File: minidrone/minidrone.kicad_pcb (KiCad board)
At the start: 2 copper layers, 45 x 150 mm, 88 parts, among them J1 GATE, J2 OUT, J3 Conn_01x10, Q1 BC337, Q2 BC337, Q3 BC337, Q4 BC337, Q5 BC337, Q6 BC377, Q7 BC377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

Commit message: Correct pot footprints. continue layout
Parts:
- R10, R2, R4, R6, R8: footprint Resistor_THT:R_Axial_DIN0207_L6.3mm_D2.5mm_P10.16mm_Horizontal -> Resistor_THT:R_Axial_DIN0207_L6.3mm_D2.5mm_P2.54mm_Vertical
- R13: value 10k -> 100k
- R15: value 47k -> 330k
- R16: footprint Resistor_THT:R_Axial_DIN0207_L6.3mm_D2.5mm_P2.54mm_Vertical -> Resistor_THT:R_Axial_DIN0207_L6.3mm_D2.5mm_P10.16mm_Horizontal
- RV1, RV2, RV3, RV4, RV5, RV6: footprint Potentiometer_THT:Potentiometer_Bourns_PTV09A-1_Single_Vertical -> minidrone:Bourns_PVT09A
- RV7, RV8: footprint Potentiometer_THT:Potentiometer_Bourns_PTV09A-1_Single_Vertical -> minidrone:Bourns_PDB12-H
- moved R11 235.9 mm to (-105.0, 147.0)
- moved R14 235.9 mm to (-107.5, 199.1)
- moved C9 225.2 mm to (148.0, 189.8), turned to 0 degrees
- moved C13 197.4 mm to (140.9, 147.2)
- moved C12 194.9 mm to (128.3, 157.4)
- moved C8 189.1 mm to (140.3, 189.8), turned to 0 degrees
- moved Q6 166.3 mm to (126.3, 130.7), turned to 90 degrees
- moved J2 99.0 mm to (153.7, 86.3)
- moved RV6 77.8 mm to (147.9, 104.7), turned to 0 degrees
- moved SW5 69.9 mm to (104.8, 189.1)
- moved SW4 66.1 mm to (104.8, 165.0)
- moved D5 65.2 mm to (116.2, 189.1), turned to 180 degrees
- moved SW3 62.4 mm to (104.8, 140.9)
- moved R10 61.5 mm to (55.0, 188.1)
- moved R4 61.5 mm to (55.0, 128.1)
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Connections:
- net /Oscillator Bank/VIN renamed /VIN
- C10 pad 2: Net-(C10-Pad2) -> GND
- C11 pad 1: Net-(C10-Pad2) -> GND
- C12 pad 2: Net-(C12-Pad2) -> GND
- C13 pad 1: Net-(C12-Pad2) -> GND
- C14 pad 2: Net-(C14-Pad2) -> GND
- C15 pad 1: Net-(C14-Pad2) -> GND
- C7 pad 1: Net-(C7-Pad1) -> /EG_CAP
- D6 pad 1: Net-(D6-Pad1) -> /EG_TRIG
- D7 pad 1: Net-(D6-Pad1) -> /EG_TRIG
- D8 pad 2: Net-(D8-Pad2) -> /EG_COMP_OUT
- D9 pad 1: Net-(D8-Pad2) -> /EG_COMP_OUT
- R13 pad 1: Net-(R13-Pad1) -> /EG_CREF
- R14 pad 1: Net-(D6-Pad1) -> /EG_TRIG
- R15 pad 2: Net-(R13-Pad1) -> /EG_CREF
- RV7 pad 2: Net-(C7-Pad1) -> /EG_CAP
- RV7 pad 3: Net-(C7-Pad1) -> /EG_CAP
- RV8 pad 2: Net-(C7-Pad1) -> /EG_CAP
- RV8 pad 3: Net-(C7-Pad1) -> /EG_CAP
- U2 pad 1: Net-(D8-Pad2) -> /EG_OUT
- U2 pad 2: Net-(R13-Pad1) -> /EG_OUT
- U2 pad 3: Net-(D6-Pad1) -> /EG_CAP
- U2 pad 5: Net-(C7-Pad1) -> /EG_TRIG
- U2 pad 6: /EG_OUT -> /EG_CREF
- U2 pad 7: /EG_OUT -> /EG_COMP_OUT
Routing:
- net /VIN: track 0.00 -> 147.3 mm
- net /EG_CAP: track 0.00 -> 31.6 mm
- net Net-(D8-Pad1): track 0.00 -> 29.4 mm
- net Net-(R1-Pad1): track 0.00 -> 26.8 mm
- net Net-(D7-Pad2): track 0.00 -> 17.4 mm
- net /EG_COMP_OUT: track 0.00 -> 15.0 mm
- net /GATE: track 0.00 -> 13.1 mm
- net Net-(C1-Pad1): track 0.00 -> 12.5 mm
- net Net-(C1-Pad2): track 0.00 -> 9.56 mm
- net Net-(Q6-Pad2): track 0.00 -> 8.46 mm
- net Net-(D9-Pad2): track 0.00 -> 7.06 mm
- net /EG_OUT: track 0.00 -> 6.88 mm
- net +12V: track 0.00 -> 5.61 mm
- net Net-(R1-Pad2): track 0.00 -> 5.22 mm
- net /EG_TRIG: track 0.00 -> 5.08 mm
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- added copper zone on B.Cu, net +12V
- added copper zone on B.Cu, net -12V
- added copper zone on F.Cu, net GND
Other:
- board size 45 x 150 mm -> 61 x 124.5 mm

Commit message: Continue layout
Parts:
- R10, R11, R13, R17, R18, R19, R2, R20, R24, R4, R6, R8: footprint Resistor_THT:R_Axial_DIN0207_L6.3mm_D2.5mm_P2.54mm_Vertical -> Resistor_THT:R_Axial_DIN0207_L6.3mm_D2.5mm_P10.16mm_Horizontal
- R14: value 100k -> 330k; footprint Resistor_THT:R_Axial_DIN0207_L6.3mm_D2.5mm_P2.54mm_Vertical -> Resistor_THT:R_Axial_DIN0207_L6.3mm_D2.5mm_P10.16mm_Horizontal
- R15: value 330k -> 100k
- moved R23 322.4 mm to (209.3, -42.2)
- moved R25 322.4 mm to (211.5, -34.1)
- moved R28 322.4 mm to (224.8, -23.8)
- moved R14 317.5 mm to (196.2, 106.8), turned to 180 degrees
- moved C15 311.8 mm to (212.1, 48.9), turned to 0 degrees
- moved C14 306.2 mm to (207.0, 36.2), turned to 0 degrees
- moved R19 304.8 mm to (224.2, 38.7), turned to -90 degrees
- moved R11 302.4 mm to (190.5, 82.6)
- moved R18 295.8 mm to (217.2, 38.7), turned to -90 degrees
- moved R21 285.6 mm to (201.3, 75.0), turned to 90 degrees
- moved Q9 282.3 mm to (199.8, 54.7), turned to -90 degrees
- moved R24 280.9 mm to (232.4, 52.7), turned to 90 degrees
- moved R30 278.8 mm to (218.7, 66.7), turned to 0 degrees
- moved Q8 273.9 mm to (203.2, 59.8), turned to 90 degrees
- moved JP1 273.9 mm to (195.6, 57.1), turned to 0 degrees
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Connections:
- R14 pad 1: /EG_TRIG -> +12V
- R14 pad 2: GND -> /EG_CREF
- R15 pad 1: +12V -> /EG_TRIG
- R15 pad 2: /EG_CREF -> GND
- U3 pad 1: Net-(R29-Pad2) -> Net-(R20-Pad2)
- U3 pad 2: Net-(R26-Pad2) -> Net-(R17-Pad2)
- U3 pad 3: Net-(R27-Pad2) -> Net-(R18-Pad1)
- U3 pad 5: Net-(R18-Pad1) -> Net-(R27-Pad2)
- U3 pad 6: Net-(R17-Pad2) -> Net-(R26-Pad2)
- U3 pad 7: Net-(R20-Pad2) -> Net-(R29-Pad2)
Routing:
- net -12V: track 0.00 -> 188.9 mm
- net +12V: track 5.61 -> 140.9 mm
- net /Oscillator Bank/OUT: track 0.00 -> 83.3 mm, vias 0 -> 1
- net Net-(R17-Pad2): track 0.00 -> 54.7 mm
- net Net-(C6-Pad1): track 0.00 -> 30.1 mm
- net Net-(C5-Pad1): track 0.00 -> 30.0 mm
- net Net-(RV6-Pad2): track 0.00 -> 29.5 mm
- net Net-(R3-Pad1): track 0.00 -> 25.0 mm
- net /EG_OUT: track 6.88 -> 28.9 mm
- net /EG_CREF: track 0.00 -> 20.9 mm
- net /EG_CAP: track 31.6 -> 52.4 mm
- net Net-(C2-Pad1): track 0.00 -> 20.6 mm
- net Net-(R9-Pad1): track 0.00 -> 20.1 mm
- net Net-(C3-Pad1): track 0.00 -> 19.9 mm
- net Net-(C4-Pad1): track 0.00 -> 19.7 mm
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- removed copper zone on B.Cu, net +12V
- removed copper zone on B.Cu, net -12V
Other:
- board size 61 x 124.5 mm -> 61 x 116.8 mm

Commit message: Complete layout
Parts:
- R12, R15, R21, R22, R25, R26, R27, R28, R29, R30: footprint Resistor_THT:R_Axial_DIN0207_L6.3mm_D2.5mm_P2.54mm_Vertical -> Resistor_THT:R_Axial_DIN0207_L6.3mm_D2.5mm_P10.16mm_Horizontal
- R23: value 20k 0.1% -> 10k; footprint Resistor_THT:R_Axial_DIN0207_L6.3mm_D2.5mm_P2.54mm_Vertical -> Resistor_THT:R_Axial_DIN0207_L6.3mm_D2.5mm_P10.16mm_Horizontal
- R24: value 10k -> 20k 0.1%
- moved R25 105.3 mm to (206.4, 71.1), turned to 90 degrees
- moved R23 90.7 mm to (216.5, 48.3), turned to 90 degrees
- moved R28 73.2 mm to (203.8, 46.4), turned to 90 degrees
- moved J2 49.1 mm to (184.2, 38.1), turned to 180 degrees
- moved R24 43.9 mm to (188.6, 55.9), turned to 0 degrees
- moved R30 36.8 mm to (198.1, 36.2), turned to 180 degrees
- moved R3 19.3 mm to (177.8, 75.6), turned to 90 degrees
- moved R26 18.5 mm to (188.6, 53.3)
- moved JP1 11.0 mm to (184.8, 59.1), turned to 90 degrees
- moved R27 9.44 mm to (206.4, 58.4)
- moved R22 7.70 mm to (203.8, 64.8)
- moved R12 6.34 mm to (200.0, 122.6)
- moved Q9 5.48 mm to (203.8, 58.4), turned to 180 degrees
- moved Q8 4.60 mm to (198.8, 61.0), turned to 0 degrees
- moved R18 4.49 mm to (221.6, 38.1)
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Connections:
- R23 pad 1: +12V -> Net-(Q8-Pad3)
- R23 pad 2: Net-(Q8-Pad1) -> Net-(R20-Pad2)
- R24 pad 1: Net-(Q8-Pad3) -> +12V
- R24 pad 2: Net-(R20-Pad2) -> Net-(Q8-Pad1)
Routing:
- net +12V: track 140.9 -> 229.6 mm, vias 0 -> 1
- net -12V: track 188.9 -> 262.7 mm, vias 0 -> 2
- net Net-(Q8-Pad3): track 0.00 -> 30.1 mm
- net Net-(Q8-Pad1): track 0.00 -> 24.5 mm
- net /VCA_BIAS: track 0.00 -> 23.4 mm, vias 0 -> 1
- net Net-(R17-Pad2): track 54.7 -> 71.6 mm
- net Net-(R26-Pad2): track 0.00 -> 14.4 mm
- net Net-(R18-Pad1): track 0.00 -> 12.3 mm
- net Net-(R29-Pad2): track 0.00 -> 11.2 mm
- net /EG_OUT: track 28.9 -> 36.3 mm
- net Net-(Q8-Pad2): track 0.00 -> 6.96 mm
- net Net-(R31-Pad1): track 0.00 -> 6.86 mm
- net /OUT: track 0.00 -> 6.40 mm
- net Net-(R3-Pad2): track 16.5 -> 10.6 mm
- net Net-(R3-Pad1): track 25.0 -> 19.3 mm
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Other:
- board size 61 x 116.8 mm -> 60.9 x 116.2 mm

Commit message: Start front panel
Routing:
- added copper zone on B.Cu, net (none)
- added copper zone on F.Cu, net (none)
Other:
- board size 60.9 x 116.2 mm -> 162.5 x 133.3 mm
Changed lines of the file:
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@@
   (gr_rect (start 217.155 146.6125) (end 219.695 149.1525) (layer "B.SilkS") (width 0.12) (fill solid))
   (gr_line (start 219.695 141.5325) (end 219.695 146.6125) (layer "B.SilkS") (width 0.12))
+  (gr_line (start 63.5 68.58) (end 129.54 68.58) (layer "Dwgs.User") (width 0.1))
+  (gr_line (start 93.98 26.035) (end 93.98 159.385) (layer "Dwgs.User") (width 0.1))
+  (gr_line (start 63.5 92.71) (end 129.54 92.71) (layer "Dwgs.User") (width 0.1))
   (gr_line (start 182.865 26.015) (end 182.865 159.365) (layer "Dwgs.User") (width 0.1))
   (gr_line (start 162.545 140.95) (end 228.585 140.95) (layer "Dwgs.User") (width 0.1))
+  (gr_line (start 116.84 26.035) (end 116.84 159.385) (layer "Dwgs.User") (width 0.1))
+  (gr_line (start 63.5 116.84) (end 129.54 116.84) (layer "Dwgs.User") (width 0.1))
+  (gr_line (start 63.5 153.055) (end 129.54 153.055) (layer "Dwgs.User") (width 0.1))
   (gr_line (start 162.545 116.82) (end 228.585 116.82) (layer "Dwgs.User") (width 0.1))
+  (gr_line (start 73.66 26.035) (end 73.66 159.385) (layer "Dwgs.User") (width 0.1))
   (gr_line (start 162.545 92.69) (end 228.585 92.69) (layer "Dwgs.User") (width 0.1))
   (gr_line (start 193.025 26.015) (end 193.025 159.365) (layer "Dwgs.User") (width 0.1))
+  (gr_line (start 63.515 44.47) (end 129.555 44.47) (layer "Dwgs.User") (width 0.1))
   (gr_line (start 215.885 26.015) (end 215.885 159.365) (layer "Dwgs.User") (width 0.1))
+  (gr_line (start 63.5 32.405) (end 129.54 32.405) (layer "Dwgs.User") (width 0.1))
+  (gr_line (start 63.5 140.97) (end 129.54 140.97) (layer "Dwgs.User") (width 0.1))
   (gr_line (start 172.705 26.015) (end 172.705 159.365) (layer "Dwgs.User") (width 0.1))
   (gr_line (start 162.545 32.385) (end 228.585 32.385) (layer "Dwgs.User") (width 0.1))
   (gr_line (start 162.545 68.56) (end 228.585 68.56) (layer "Dwgs.User") (width 0.1))
+  (gr_line (start 83.82 26.035) (end 83.82 159.385) (layer "Dwgs.User") (width 0.1))
   (gr_line (start 162.545 153.035) (end 228.585 153.035) (layer "Dwgs.User") (width 0.1))
   (gr_rect (start 162.545 26.015) (end 228.585 159.365) (layer "Dwgs.User") (width 0.1) (fill none))
   (gr_line (start 162.56 44.45) (end 228.6 44.45) (layer "Dwgs.User") (width 0.1))
   (gr_rect (start 165.1 34.27) (end 226.045 150.495) (layer "Edge.Cuts") (width 0.05) (fill none))
+  (gr_rect (start 63.5 26.035) (end 129.54 159.385) (layer "Edge.Cuts") (width 0.1) (fill none))
   (segment (start 181.635 44.47) (end 181.595 44.43) (width 0.5) (layer "B.Cu") (net 1))
   (segment (start 181.61 48.935) (end 181.65 48.895) (width 0.5) (layer "B.Cu") (net 1))
@@
   (segment (start 193.025 123.82) (end 195.525 123.82) (width 0.5) (layer "B.Cu") (net 18))
   (segment (start 193.04 116.915) (end 193.025 116.93) (width 0.5) (layer "B.Cu") (net 18))
-  (segment (start 191.135 149.86) (end 181.535 149.86) (width 0.5) (layer "B.Cu") (net 19))
+  (segment (start 191.575489 149.399511) (end 181.074511 149.399511) (width 0.5) (layer "B.Cu") (net 19))
+  (segment (start 193.025 147.95) (end 191.575489 149.399511) (width 0.5) (layer "B.Cu") (net 19))
+  (segment (start 181.074511 149.399511) (end 177.8 146.125) (width 0.5) (layer "B.Cu") (net 19))
   (segment (start 195.525 147.95) (end 193.025 147.95) (width 0.5) (layer "B.Cu") (net 19))
-  (segment (start 193.025 147.95) (end 191.135 149.84) (width 0.5) (layer "B.Cu") (net 19))
-  (segment (start 191.135 149.84) (end 191.135 149.86) (width 0.5) (layer "B.Cu") (net 19))
-  (segment (start 181.535 149.86) (end 177.8 146.125) (width 0.5) (layer "B.Cu") (net 19))
   (segment (start 212.075 85.07) (end 205.735 85.07) (width 0.5) (layer "B.Cu") (net 20))
   (segment (start 215.885 63.495) (end 215.885 81.26) (width 0.5) (layer "B.Cu") (net 20))
@@
   (segment (start 180.34 82.625) (end 186.69 82.625) (width 0.5) (layer "F.Cu") (net 59))
   (segment (start 175.895 82.625) (end 180.34 82.625) (width 0.5) (layer "B.Cu") (net 59))
+  (zone (net 0) (net_name "") (layers F&B.Cu) (hatch edge 0.508)
+    (connect_pads (clearance 0.508))
+    (min_thickness 0.254) (filled_areas_thickness no)
+    (fill yes (thermal_gap 0.508) (thermal_bridge_width 0.508))
+    (polygon
+      (pts
+        (xy 129.54 159.385)
+        (xy 63.5 159.385)
+        (xy 63.5 26.035)
+        (xy 129.54 26.035)
+      )
+    )
+  )
   (zone (net 12) (net_name "GND") (layer "F.Cu") (hatch edge 0.508)
     (connect_pads (clearance 0.508))

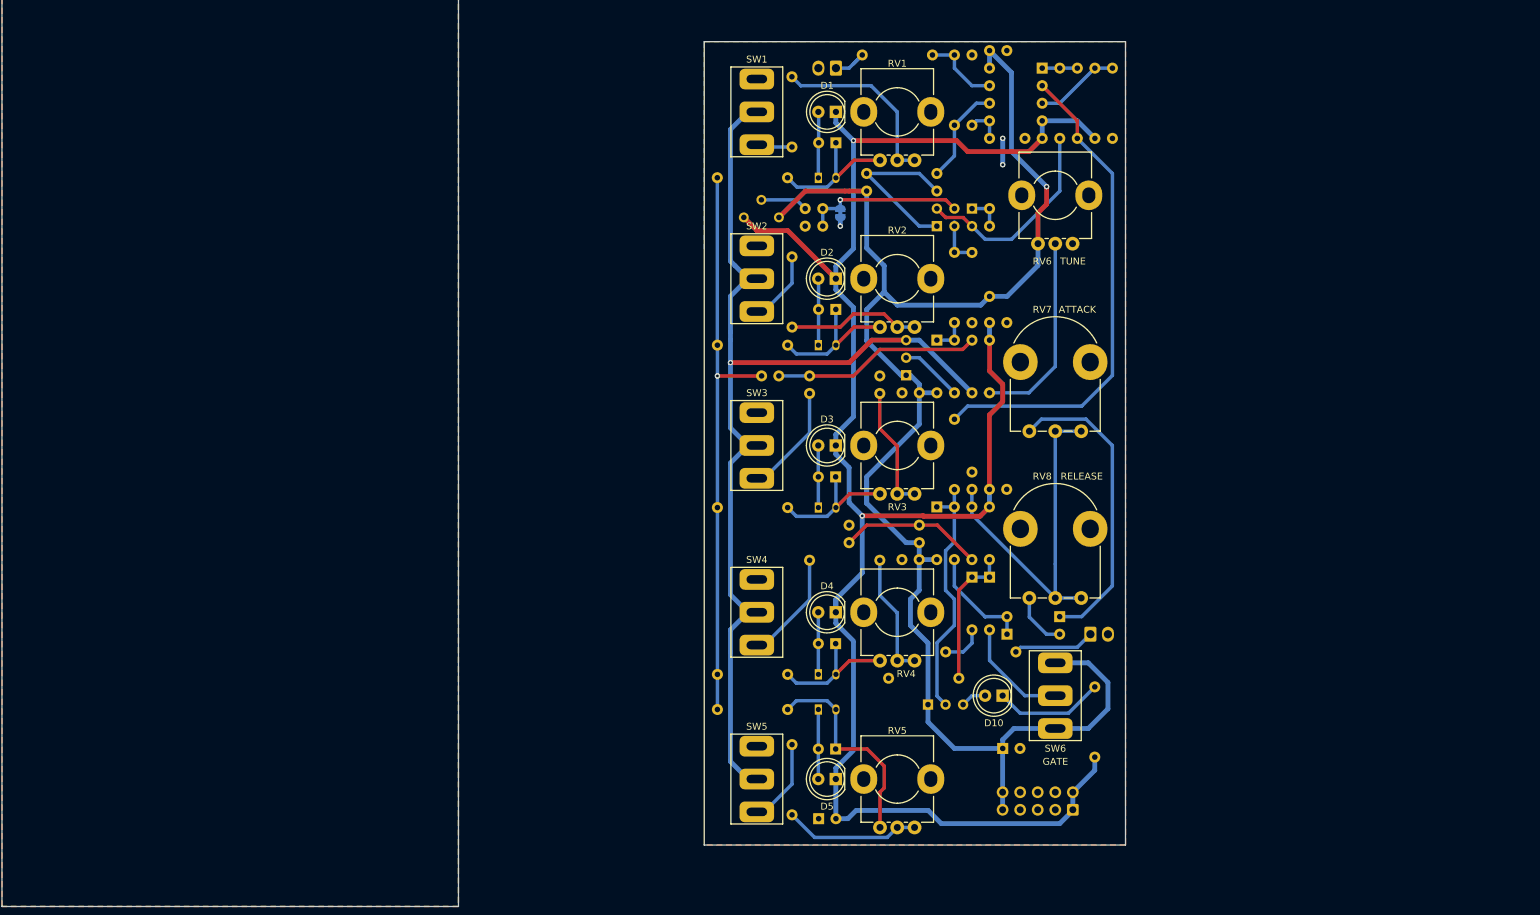
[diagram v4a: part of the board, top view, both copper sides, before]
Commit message: Lay out front panel. WIP updating mainboard layout
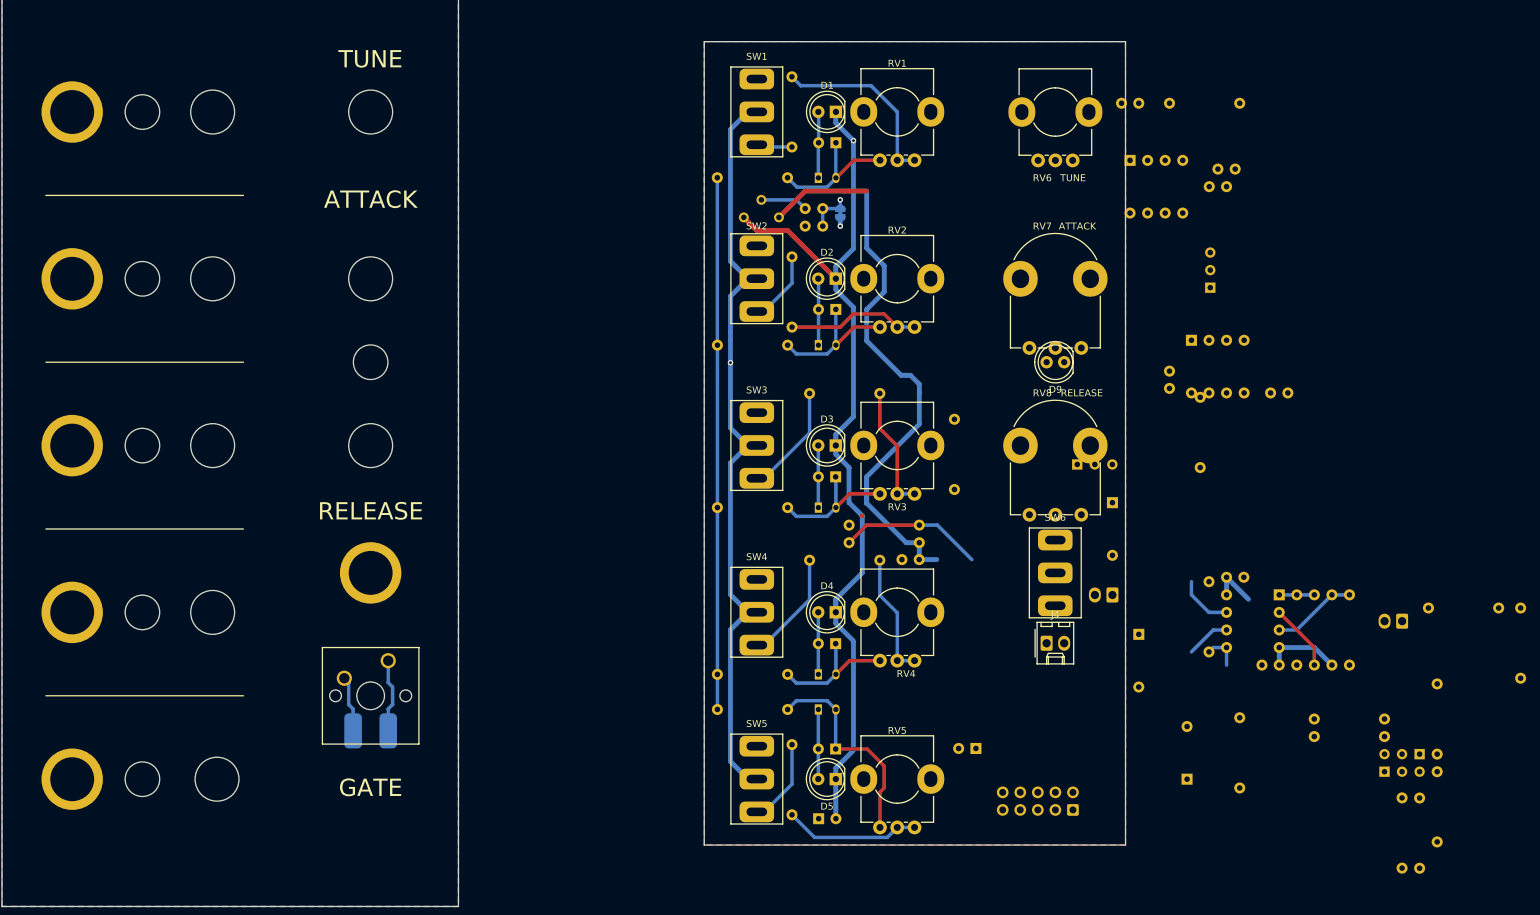
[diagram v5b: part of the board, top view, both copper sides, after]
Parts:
- removed D10: LED, LED_THT:LED_D5.0mm
- removed R12: 100k, Resistor_THT:R_Axial_DIN0207_L6.3mm_D2.5mm_P10.16mm_Horizontal
- added H1: OSC1 Enable, kosmo-lib:Hole_Toggle_Switch, F.Cu at (73.7, 44.5)
- added H10: OSC5 LED, kosmo-lib:Hole_LED_5mm, F.Cu at (83.8, 141.0)
- added H11: OSC1 Tuning, kosmo-lib:Hole_Pot, F.Cu at (94.0, 44.5)
- added H12: OSC2 Tuning, kosmo-lib:Hole_Pot, F.Cu at (94.0, 68.6)
- added H13: OSC3 Tuning, kosmo-lib:Hole_Pot, F.Cu at (94.0, 92.7)
- added H14: OSC4 Tuning, kosmo-lib:Hole_Pot, F.Cu at (94.0, 116.8)
- added H15: OSC5 Tuning, kosmo-lib:Hole_Pot, F.Cu at (94.6, 141.0)
- added H16: TUNE, kosmo-lib:Hole_Pot, F.Cu at (116.8, 44.5)
- added H17: ATTACK, kosmo-lib:Hole_Pot, F.Cu at (116.8, 68.6)
- added H18: RELEASE, kosmo-lib:Hole_Pot, F.Cu at (116.8, 92.7)
- added H19: EG LED, kosmo-lib:Hole_LED_5mm, F.Cu at (116.8, 80.6)
- added H2: OSC2 Enable, kosmo-lib:Hole_Toggle_Switch, F.Cu at (73.7, 68.6)
- added H20: Gate Toggle SW, kosmo-lib:Hole_Toggle_Switch, F.Cu at (116.8, 111.1)
- added H3: OSC3 Enable, kosmo-lib:Hole_Toggle_Switch, F.Cu at (73.7, 92.7)
- added H4: OSC4 Enable, kosmo-lib:Hole_Toggle_Switch, F.Cu at (73.7, 116.8)
- added H5: OSC5 Enable, kosmo-lib:Hole_Toggle_Switch, F.Cu at (73.7, 141.0)
- added H6: OSC1 LED, kosmo-lib:Hole_LED_5mm, F.Cu at (83.8, 44.5)
- added H7: OSC2 LED, kosmo-lib:Hole_LED_5mm, F.Cu at (83.8, 68.6)
- added H8: OSC3 LED, kosmo-lib:Hole_LED_5mm, F.Cu at (83.8, 92.7)
- added H9: OSC4 LED, kosmo-lib:Hole_LED_5mm, F.Cu at (83.8, 116.8)
- added J4: GATE, Connector_Molex:Molex_KK-254_AE-6410-02A_1x02_P2.54mm_Vertical, F.Cu at (214.6, 121.3)
- added J5: GATE, minidrone:SMD_Connector, B.Cu at (116.8, 134.0)
- added SW7: GATE, Button_Switch_Keyboard:SW_Cherry_MX_1.00u_PCB, F.Cu at (119.4, 123.8)
- C1: value 10uF -> 1uF
- C5: value 1uF -> 10uF
- D6, D7, D8: value D -> 1N914
- D9: value D -> LED; footprint Diode_THT:D_DO-35_SOD27_P7.62mm_Horizontal -> LED_THT:LED_D5.0mm; moved to F.Cu
- J1: value GATE -> Conn_01x10; footprint Connector_Molex:Molex_KK-254_AE-6410-02A_1x02_P2.54mm_Vertical -> Connector_IDC:IDC-Header_2x05_P2.54mm_Vertical
- J3: value Conn_01x10 -> EXT GATE; footprint Connector_IDC:IDC-Header_2x05_P2.54mm_Vertical -> Connector_Molex:Molex_KK-254_AE-6410-02A_1x02_P2.54mm_Vertical
- SW1, SW2, SW3, SW4, SW5: footprint modular:Switch_SPDT -> kosmo-lib:Switch_SPDT
- SW6: value GATE -> GATE_LATCH; footprint modular:Switch_SPDT -> kosmo-lib:Switch_SPDT
- moved R30 114.5 mm to (280.0, 116.2)
- moved J2 114.5 mm to (266.1, 118.1)
- moved R29 114.5 mm to (283.2, 126.4)
- moved R21 102.1 mm to (266.1, 153.8)
- moved Q9 102.1 mm to (268.6, 137.3)
- moved R22 102.1 mm to (268.6, 143.7)
- moved R24 102.1 mm to (253.4, 134.8)
- moved Q8 102.1 mm to (263.5, 139.9)
- moved R25 102.1 mm to (271.1, 150.0)
- moved R26 102.1 mm to (253.4, 132.3)
- moved R27 102.1 mm to (271.1, 137.3)
- moved R28 83.6 mm to (238.1, 122.6)
- moved C14 83.6 mm to (240.7, 111.8)
- moved R20 83.6 mm to (253.4, 124.5)
- moved C15 83.6 mm to (245.8, 124.5)
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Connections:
- net /EG_CREF renamed /EG_VTH
- net Net-(RV6-Pad2) renamed /CV
- D6 pad 2: Net-(D6-Pad2) -> /EXT_GATE
- D7 pad 1: /EG_TRIG -> Net-(D7-Pad1)
- D7 pad 2: Net-(D7-Pad2) -> /EG_COMP_OUT
- D8 pad 1: Net-(D8-Pad1) -> /EG_COMP_OUT
- D8 pad 2: /EG_COMP_OUT -> Net-(D8-Pad2)
- D9 pad 1: /EG_COMP_OUT -> Net-(D9-Pad1)
- J1 pad 1: /GATE -> -12V
- J1 pad 2: GND -> -12V
- J3 pad 1: -12V -> /EXT_GATE
- J3 pad 2: -12V -> GND
- Q7 pad 3: Net-(D10-Pad2) -> Net-(D9-Pad2)
- R16 pad 1: Net-(D10-Pad1) -> Net-(D9-Pad1)
- RV7 pad 1: Net-(D8-Pad1) -> Net-(D7-Pad1)
- RV8 pad 1: Net-(D9-Pad2) -> Net-(D8-Pad2)
- SW6 pad 1: +12V -> unconnected-(SW6-Pad1)
- SW6 pad 2: Net-(D7-Pad2) -> /EG_TRIG
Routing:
- net +12V: track 229.6 -> 93.8 mm, vias 1 -> 0
- net -12V: track 262.7 -> 141.3 mm, vias 2 -> 1
- net Net-(R17-Pad2): track 71.6 -> 9.72 mm
- net /EG_CAP: track 52.3 -> 0.00 mm
- net Net-(D8-Pad1): track 44.1 -> 0.00 mm
- net /VIN: track 152.6 -> 113.2 mm
- net /EG_OUT: track 36.3 -> 0.02 mm
- net Net-(Q8-Pad3): track 30.1 -> 0.00 mm
- net Net-(C6-Pad1): track 30.1 -> 0.00 mm
- net /CV: track 29.5 -> 0.00 mm
- net Net-(Q8-Pad1): track 24.5 -> 0.00 mm
- net /EG_TRIG: track 20.5 -> 0.00 mm
- net /VCA_BIAS: track 23.4 -> 6.35 mm
- net Net-(D7-Pad2): track 16.0 -> 0.00 mm
- net Net-(D10-Pad1): track 16.0 -> 0.00 mm
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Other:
- board text added: "FRONT PANEL"
- board text added: "GATE"
- board text added: "MAINBOARD"
